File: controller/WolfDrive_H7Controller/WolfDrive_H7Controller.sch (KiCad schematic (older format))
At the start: 319 parts, among them CN10 CONN_02X17, CN7 CONN_02X10, CN8 CONN_02X08, CN9 CONN_02X15, CON1 SD_Card, J1 USB_OTG, J10 GND, J11 GND, J12 5V, J13 Regen, J14 Throttle, J15 PWM1, J16 PWM2, J17 PWM3, J18 ~PWM1, J19 ~PWM2, J2 QSPI_CLK, J20 ~PWM3, J21 OCV, J22 ~F_C, J23 ~F_B, J24 ~F_A, J25 Overtemp, J26 PWM_EN, J27 Conn_01x04_Female, J28 GS3, J29 Conn_01x04, J3 QSPI_NCS, J30 SPI2_SCK, J31 SPI2_NSS, J32 SPI2_MOSI, J33 SPI2_MISO, J34 PS-DIS, J35 3V3, J36 GND, J37 GND, J38 AGND, J39 SP1_MISO, J4 QSPI_IO0, J40 SP1_SCK, J41 SP1_NSS, J42 SP1_MOSI, J43 GS3, J44 GS3, J45 GS3, J46 GS3, J47 GS3, J48 GS3, J49 GS3, J5 QSPI_IO1, J50 GS3, J51 GS3, J52 GS3, J53 GS3, J54 GS3, J55 GS3, J6 QSPI_IO2, J7 QSPI_IO3, J8 12V, J9 GND, P1 GATE_IO_A, P10 GATE_IO_A, P11 GATE_IO_A, P7 CONN_01X02, P9 GATE_IO_A, U1 LM1117-5.0, U10 74HC266, U11 FT232RL, U12 74LVC1G02, U13 74LVC1G02, U14 74LVC1G02, U15 74LVC1G02, U16 74LVC1G02, U17 74LVC1G02, U18 74LVC1G02, U19 74LVC1G02, U2 LM1117-3.3, U21 74LVC1G02, U3 MCP101-315D, U4 LTV-356T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

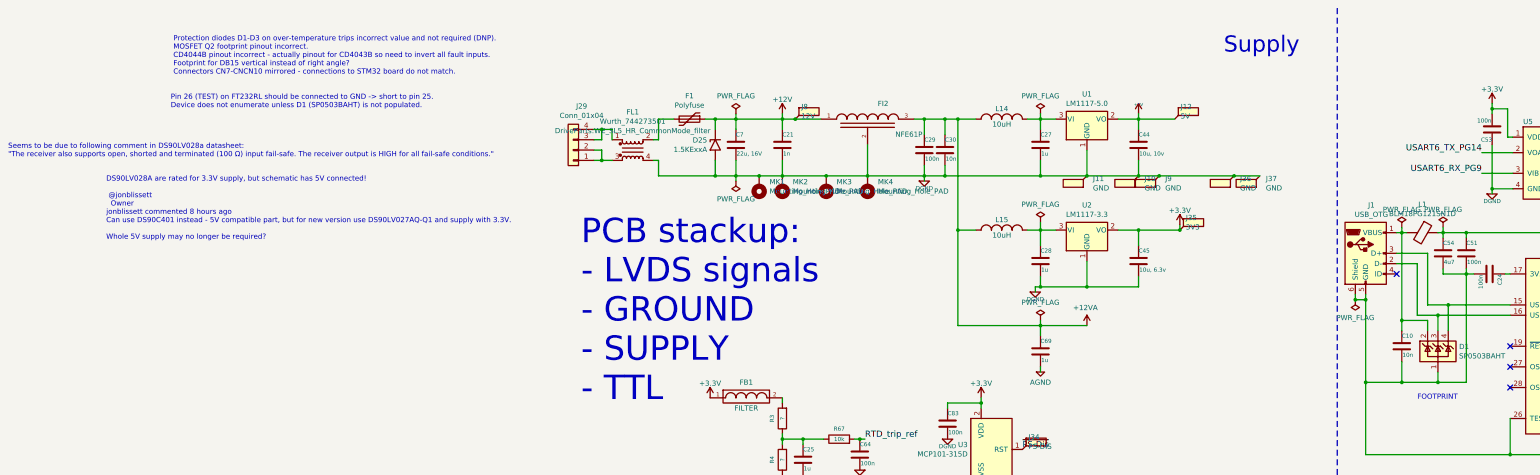
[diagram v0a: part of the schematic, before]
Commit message: Finished layout, silk sceen amended
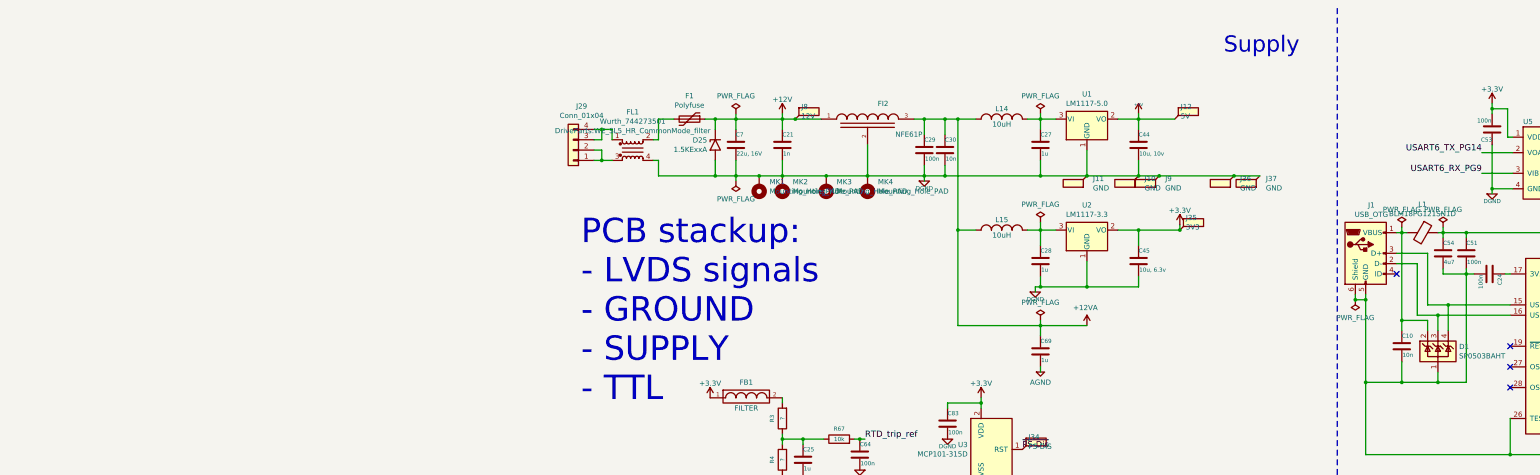
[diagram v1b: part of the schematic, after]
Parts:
- D1: footprint TO_SOT_Packages_SMD:SOT-143 -> Package_TO_SOT_SMD:SOT-143R_Reverse_Handsoldering
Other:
- note removed: "DS90LV028A are rated for 3.3V supply, but schematic has 5V connected!\n\n @jonblissett\n Owner\njonblissett commented 8 hours ago\nCan use DS90C401 instead - 5V compatible part, but for new version use DS90LV027AQ-Q1 and supply with 3.3V.\n\nWhole 5V supply may no longer be required?"
- note removed: "FOOTPRINT"
- note removed: "Pin 26 (TEST) on FT232RL should be connected to GND -> short to pin 25.\nDevice does not enumerate unless D1 (SP0503BAHT) is not populated."
- note removed: "Protection diodes D1-D3 on over-temperature trips incorrect value and not required (DNP).\nMOSFET Q2 footprint pinout incorrect.\nCD4044B pinout incorrect - actually pinout for CD4043B so need to invert all fault inputs.\nFootprint for DB15 vertical instead of right angle?\nConnectors CN7-CNCN10 mirrored - connections to STM32 board do not match."
- note removed: "Seems to be due to following comment in DS90LV028a datasheet:\n"The receiver also supports open, shorted and terminated (100 Ω) input fail-safe. The receiver output is HIGH for all fail-safe conditions.""
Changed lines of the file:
@@
 F 0 "D1" H 9455 3846 50  0000 L CNN
 F 1 "SP0503BAHT" H 9455 3755 50  0000 L CNN
-F 2 "TO_SOT_Packages_SMD:SOT-143" H 9475 3750 50  0001 L CNN
+F 2 "Package_TO_SOT_SMD:SOT-143R_Reverse_Handsoldering" H 9475 3750 50  0001 L CNN
 F 3 "http://www.littelfuse.com/~/media/files/littelfuse/technical%20resources/documents/data%20sheets/sp05xxba.pdf" H 9375 3925 50  0001 C CNN
 	1    9250 3800
@@
 Wire Wire Line
 	10250 10900 10250 10950
-Text Notes 9050 4275 0    50   ~ 0
-FOOTPRINT
 $Comp
 L Jumper:SolderJumper_3_Bridged12 J28
@@
 	1    0    0    -1
 $EndComp
-Text Notes -3025 1450 0    50   ~ 0
-Pin 26 (TEST) on FT232RL should be connected to GND -> short to pin 25.\nDevice does not enumerate unless D1 (SP0503BAHT) is not populated.
-Text Notes -4600 1925 0    50   ~ 0
-Seems to be due to following comment in DS90LV028a datasheet:\n"The receiver also supports open, shorted and terminated (100 Ω) input fail-safe. The receiver output is HIGH for all fail-safe conditions."
-Text Notes -3000 1125 0    50   ~ 0
-Protection diodes D1-D3 on over-temperature trips incorrect value and not required (DNP).\nMOSFET Q2 footprint pinout incorrect.\nCD4044B pinout incorrect - actually pinout for CD4043B so need to invert all fault inputs.\nFootprint for DB15 vertical instead of right angle?\nConnectors CN7-CNCN10 mirrored - connections to STM32 board do not match.
-Text Notes -3650 2725 0    50   ~ 0
-DS90LV028A are rated for 3.3V supply, but schematic has 5V connected!\n\n @jonblissett\n  Owner\njonblissett commented 8 hours ago\nCan use DS90C401 instead - 5V compatible part, but for new version use DS90LV027AQ-Q1 and supply with 3.3V.\n\nWhole 5V supply may no longer be required?
 Wire Wire Line
 	1150 1850 1150 1950

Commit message: Library fix for KiCAD v5
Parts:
- added U?: OPA2340, Housings_SOIC:SOIC-8_3.9x4.9mm_Pitch1.27mm, symbol Amplifier_Operational:OPA2340
- J1: symbol Connector_Specialized:USB_OTG -> Connector:USB_OTG
- J10, J11, J12, J13, J14, J15, J16, J17, J18, J19, J2, J20, J21, J22, J23, J24, J25, J26, J3, J30, J31, J32, J33, J34, J35, J36, J37, J38, J39, J4, J40, J41, J42, J5, J6, J7, J8, J9: symbol Connector_Specialized:Test_Point_Flag -> Connector:Test_Point_Flag
- J27: symbol Connector_Specialized:Conn_01x04_Female -> Connector:Conn_01x04_Female
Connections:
- net +12V: no longer J8.1
- net 12V_thr: now also U?.8 (V+)
- net AGND: now also U?.4 (V-)
- net DGND: no longer J36.1, J9.1
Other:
- note added: "ALL GATES ON FIBERS SHOULD BE XNOR!"
- moved on the sheet: C59, C63, C70, C71, C72, D6, FI4, J14, J27, J38, L16, R29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
